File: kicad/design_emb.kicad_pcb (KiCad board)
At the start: 2 copper layers, 79.8 x 98.9 mm, 123 parts, among them J1 Conn_01x04, J2 Barrel_Jack, J3 USB_A, J4 Conn_01x03, J5 Conn_02x11_Counter_Clockwise, J6 Conn_02x10_Counter_Clockwise, J7 Screw_Terminal_01x02, J8 Screw_Terminal_01x02, K1 SANYOU_SRD_Form_C, K2 SANYOU_SRD_Form_C, Q1 MMBT3904, Q2 MMBT3904, SW1 SW_Push, SW3 SW_Push, U1 SRX.X.TCT, U10 S25FL116KOXNFIQ-11, U2 SRX.X.TCT, U3 STM32F446ZETx, U4 ICE40HX1K, U5 TLV1117LV33DCYR, U6 TLV1117LV33DCYR, U7 TLV1117LV12DCYR, U8 OMEGA2, U9 RCLAMP0502B

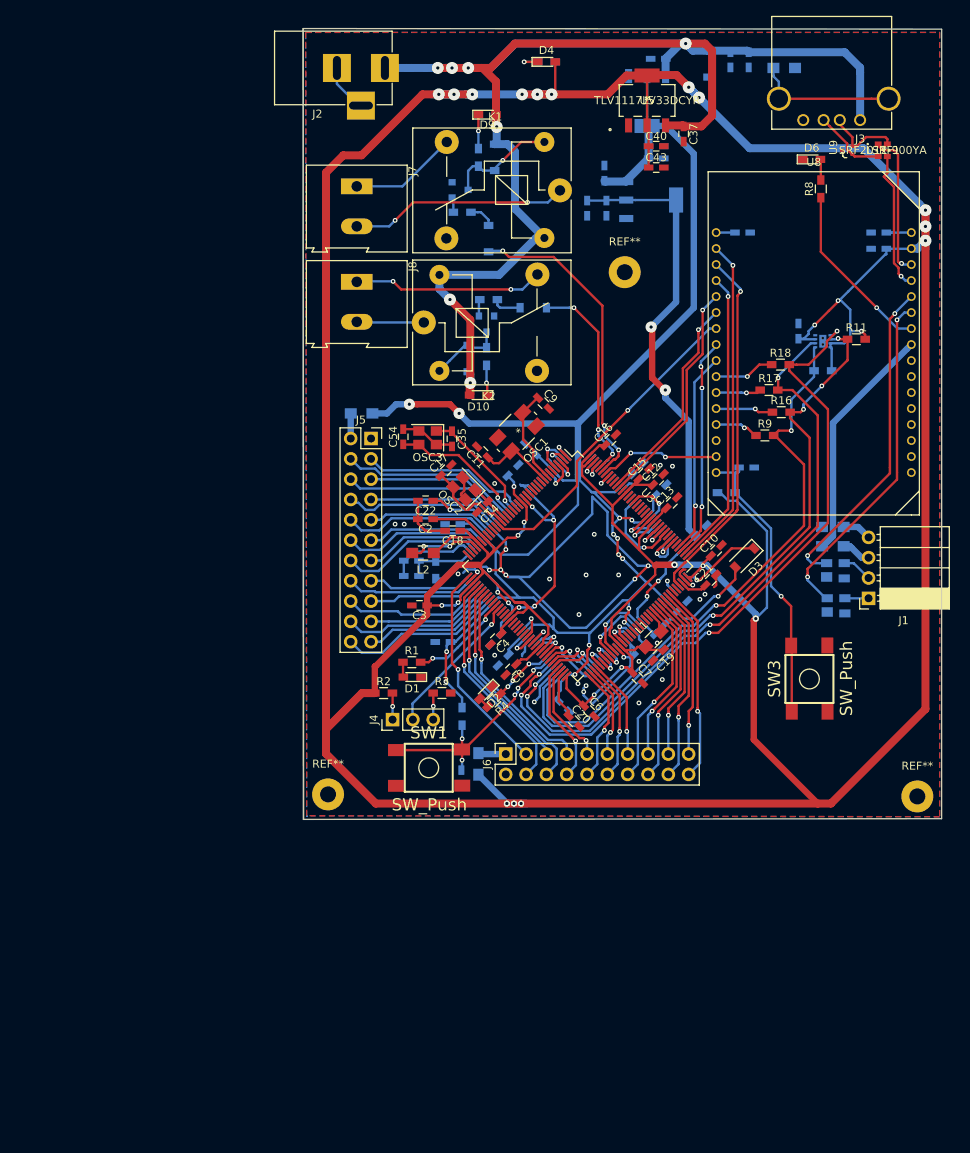
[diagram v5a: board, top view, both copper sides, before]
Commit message: correcciones silk
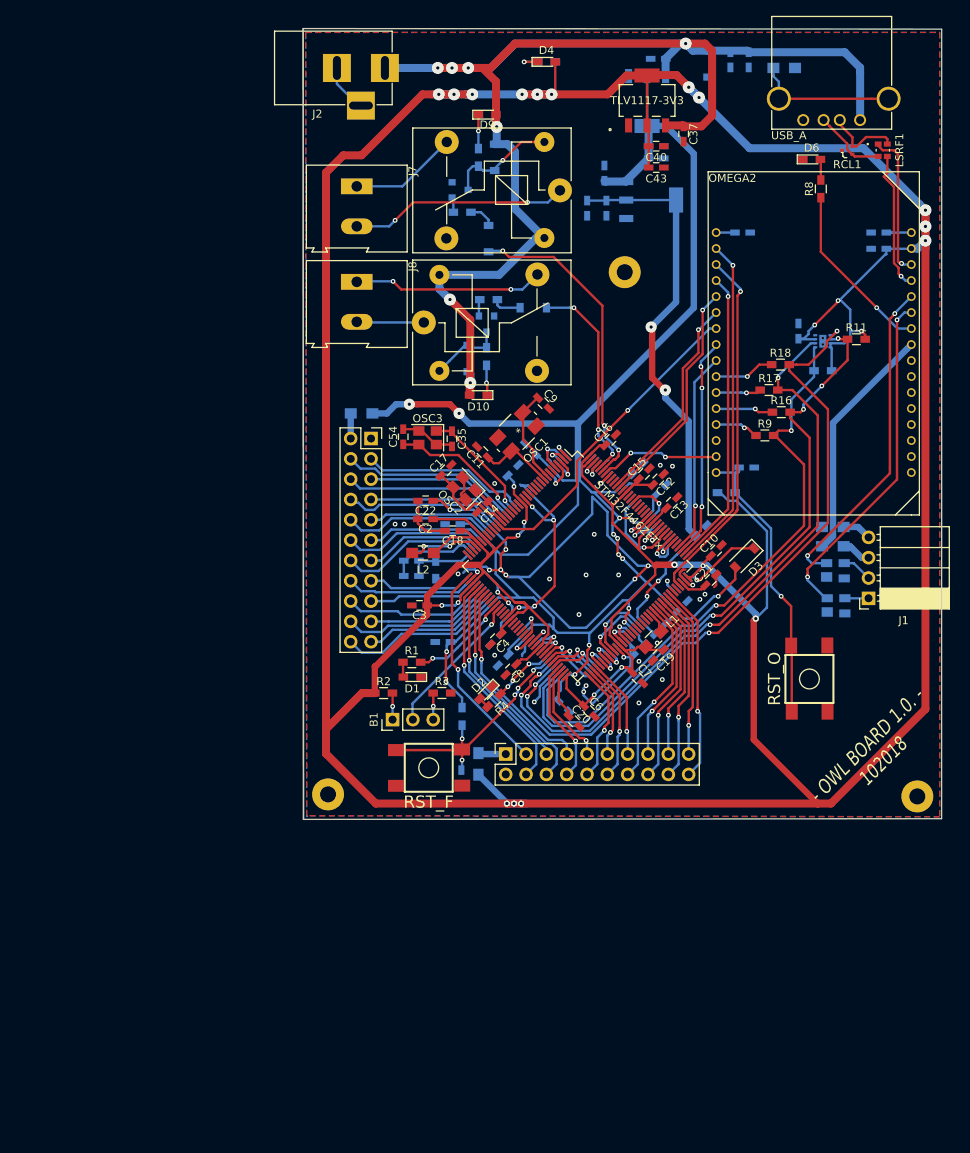
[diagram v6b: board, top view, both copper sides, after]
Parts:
- U5, U6: value TLV1117LV33DCYR -> TLV1117-3V3
- U7: value TLV1117LV12DCYR -> TLV1117-1V2
- renumbered J4 to B1, U4 to ICE40HX1K, U8 to OMEGA2, U9 to RCL1, SW1 to RST_F, SW3 to RST_O, U1 to SRX.X., U2 to SRX.X., U3 to STM32F446ZETx, J3 to USB_A
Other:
- board text added: "- OWL BOARD 1.0. - 102018"

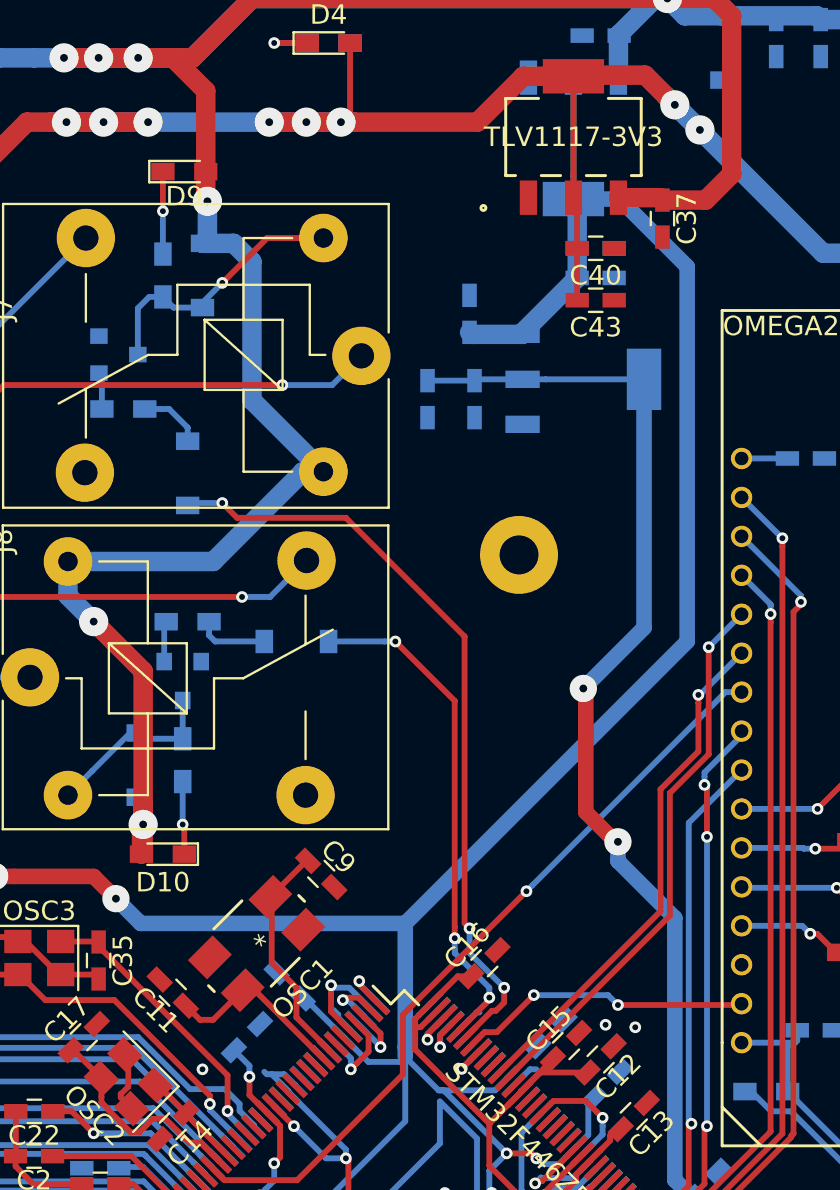
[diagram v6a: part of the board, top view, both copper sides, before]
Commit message: cambio osc1 stm32
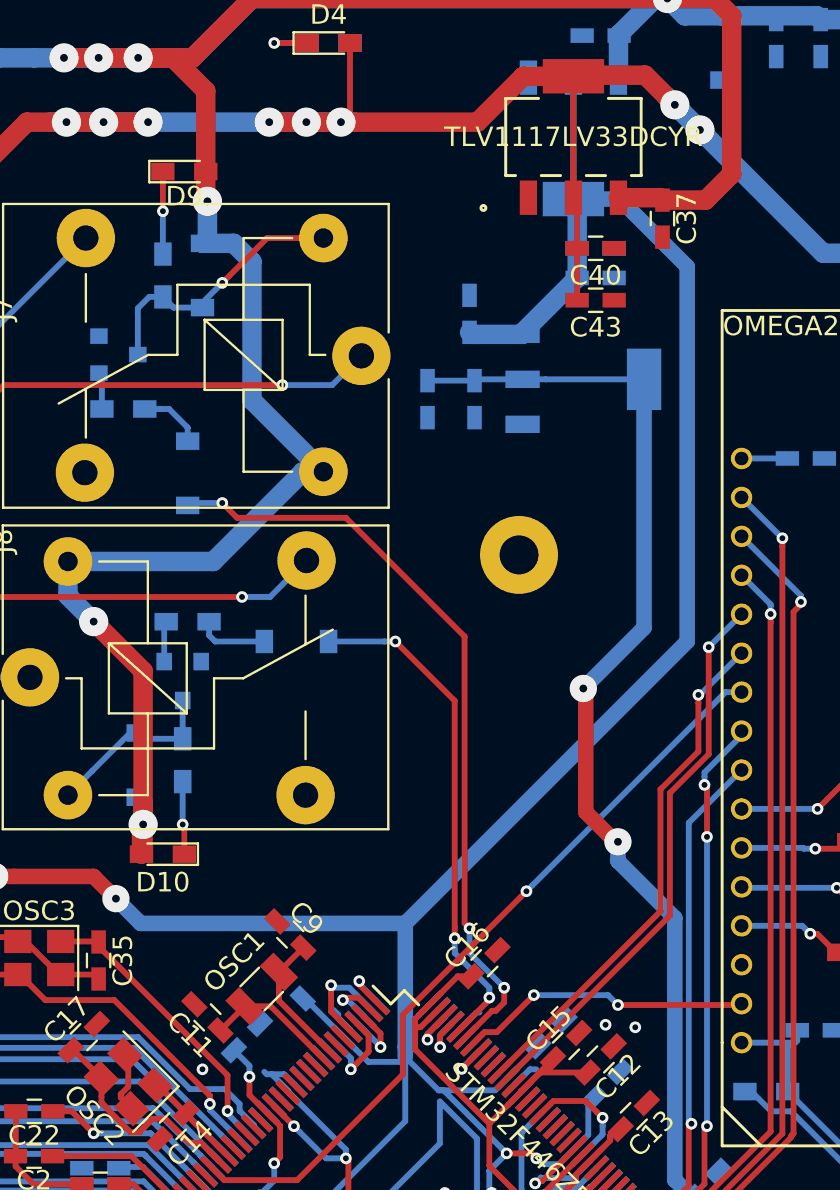
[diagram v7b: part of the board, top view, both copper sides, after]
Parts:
- C11, C9: value 18pF -> 9pF
- OSC1: value 32.768MHz -> 32,768K; footprint ABMM2-32.768MHZ:ABMM2-32.768MHZ-E2F-T -> Crystal:Crystal_SMD_3215-2Pin_3.2x1.5mm
- U5, U6: value TLV1117-3V3 -> TLV1117LV33DCYR
- U7: value TLV1117-1V2 -> TLV1117LV12DCYR
- moved C9 3.49 mm to (139.9, 94.3), turned to 135 degrees
- moved OSC1 2.37 mm to (138.4, 97.1), turned to 45 degrees
- moved C11 2.18 mm to (135.6, 98.6)
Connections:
- OSC1 pad 2: GND -> /Sheet1/OSC32_OUT
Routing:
- net /Sheet1/OSC32_IN: track 11.9 -> 6.91 mm
- net /Sheet1/OSC32_OUT: track 9.38 -> 6.85 mm
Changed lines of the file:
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@@
     (thickness 1.6)
     (drawings 7)
-    (tracks 1758)
+    (tracks 1753)
     (zones 0)
     (modules 123)
@@
   )
   (page A4)
+  (title_block
+    (title "OWL_BOARD 1.0.")
+    (date 10/2018)
+    (company "Fabio Segura")
+    (comment 1 "de la Maestría en Ingeniería Electrónica de la Universidad Nacional de Colombia")
+    (comment 2 "Tarjeta diseñada para la asiganatura \"Diseño e implementación de sistemas embebidos\"")
+  )
   (layers
     (0 F.Cu signal)
@@
     (add_net "Net-(U8-Pad24)")
   )
+  (module Crystal:Crystal_SMD_3215-2Pin_3.2x1.5mm (layer F.Cu)
+    (at 138.424883 97.096617 45)
+    (descr "SMD Crystal FC-135 https://support.epson.biz/td/api/doc_check.php?dl=brief_FC-135R_en.pdf")
+    (tags "SMD SMT Crystal")
+    (attr smd)
+    (fp_text reference OSC1 (at 0 -2 45) (layer F.SilkS)
+      (effects (font (size 1 1) (thickness 0.15)))
+    )
+    (fp_text value 32,768K (at 0 2 45) (layer F.Fab)
+      (effects (font (size 1 1) (thickness 0.15)))
+    )
+    (fp_line (start 2 -1.15) (end 2 1.15) (layer F.CrtYd) (width 0.05))
+    (fp_line (start -2 -1.15) (end -2 1.15) (layer F.CrtYd) (width 0.05))
+    (fp_line (start -2 1.15) (end 2 1.15) (layer F.CrtYd) (width 0.05))
+    (fp_line (start -1.6 0.75) (end 1.6 0.75) (layer F.Fab) (width 0.1))
+    (fp_line (start -1.6 -0.75) (end 1.6 -0.75) (layer F.Fab) (width 0.1))
+    (fp_line (start 1.6 -0.75) (end 1.6 0.75) (layer F.Fab) (width 0.1))
+    (fp_line (start -0.675 -0.875) (end 0.675 -0.875) (layer F.SilkS) (width 0.12))
+    (fp_line (start -0.675 0.875) (end 0.675 0.875) (layer F.SilkS) (width 0.12))
+    (fp_line (start -1.6 -0.75) (end -1.6 0.75) (layer F.Fab) (width 0.1))
+    (fp_line (start -2 -1.15) (end 2 -1.15) (layer F.CrtYd) (width 0.05))
+    (fp_text user %R (at 0 -2 45) (layer F.Fab)
+      (effects (font (size 1 1) (thickness 0.15)))
+    )
+    (pad 2 smd rect (at -1.25 0 45) (size 1 1.8) (layers F.Cu F.Paste F.Mask)
+      (net 3 /Sheet1/OSC32_OUT))
+    (pad 1 smd rect (at 1.25 0 45) (size 1 1.8) (layers F.Cu F.Paste F.Mask)
+      (net 2 /Sheet1/OSC32_IN))
+    (model ${KISYS3DMOD}/Crystal.3dshapes/Crystal_SMD_3215-2Pin_3.2x1.5mm.wrl
+      (at (xyz 0 0 0))
+      (scale (xyz 1 1 1))
+      (rotate (xyz 0 0 0))
+    )
+  )
   (module Wire_Pads:SolderWirePad_single_2mmDrill (layer F.Cu)
     (at 151.638 74.803)
@@
   )
   (module Capacitors_SMD:C_0603_HandSoldering (layer F.Cu)
-    (at 141.478 91.186 315)
+    (at 139.8905 94.2975 135)
     (descr "Capacitor SMD 0603, hand soldering")
     (tags "capacitor 0603")
     (attr smd)
-    (fp_text reference C9 (at 0 -1.25 315) (layer F.SilkS)
+    (fp_text reference C9 (at 0 1.167433 135) (layer F.SilkS)
       (effects (font (size 1 1) (thickness 0.15)))
     )
-    (fp_text value 18pF (at 0 1.5 315) (layer F.Fab)
+    (fp_text value 9pF (at 0 1.5 135) (layer F.Fab)
       (effects (font (size 1 1) (thickness 0.15)))
     )
-    (fp_text user %R (at 0 -1.249999 315) (layer F.Fab)
+    (fp_text user %R (at 0 -1.249999 135) (layer F.Fab)
       (effects (font (size 1 1) (thickness 0.15)))
     )
@@
     (fp_line (start 1.8 0.65) (end 1.8 -0.65) (layer F.CrtYd) (width 0.05))
     (fp_line (start 1.8 0.65) (end -1.8 0.65) (layer F.CrtYd) (width 0.05))
-    (pad 1 smd rect (at -0.949999 0 315) (size 1.2 0.75) (layers F.Cu F.Paste F.Mask)
+    (pad 1 smd rect (at -0.949999 0 135) (size 1.2 0.75) (layers F.Cu F.Paste F.Mask)
       (net 2 /Sheet1/OSC32_IN))
-    (pad 2 smd rect (at 0.949999 0 315) (size 1.2 0.75) (layers F.Cu F.Paste F.Mask)
+    (pad 2 smd rect (at 0.949999 0 135) (size 1.2 0.75) (layers F.Cu F.Paste F.Mask)
       (net 1 GND))
     (model Capacitors_SMD.3dshapes/C_0603.wrl
@@
   )
   (module Capacitors_SMD:C_0603_HandSoldering (layer F.Cu)
-    (at 133.858 97.282 135)
+    (at 135.636 98.552 135)
     (descr "Capacitor SMD 0603, hand soldering")
     (tags "capacitor 0603")
@@
       (effects (font (size 1 1) (thickness 0.15)))
     )
-    (fp_text value 18pF (at 0 1.5 135) (layer F.Fab)
+    (fp_text value 9pF (at 0 1.5 135) (layer F.Fab)
       (effects (font (size 1 1) (thickness 0.15)))
     )
@@
       (net 30 "Net-(J3-Pad2)"))
   )
-  (module ABMM2-32.768MHZ:ABMM2-32.768MHZ-E2F-T (layer F.Cu)
-    (at 138.176 94.742 225)
-    (fp_text reference OSC1 (at 0 -3.302 45) (layer F.SilkS)
-      (effects (font (size 1 1) (thickness 0.15)))
-    )
-    (fp_text value 32.768MHz (at 0 3.429 45) (layer F.SilkS) hide
-      (effects (font (size 1 1) (thickness 0.15)))
-    )
-    (fp_text user "Copyright 2016 Accelerated Designs. All rights reserved." (at 0.025401 0 -45) (layer Cmts.User)
-      (effects (font (size 0.127 0.127) (thickness 0.002)))
-    )
-    (fp_text user * (at 0.025401 0 -45) (layer F.SilkS)
-      (effects (font (size 1 1) (thickness 0.15)))
-    )
-    (fp_text user * (at 0.025401 0 -45) (layer F.Fab)
-      (effects (font (size 1 1) (thickness 0.15)))
-    )
-    (fp_line (start 3.302001 0.214047) (end 3.302001 -0.214047) (layer F.SilkS) (width 0.1524))
-    (fp_line (start 1.047989 -2.0828) (end -0.997189 -2.0828) (layer F.SilkS) (width 0.1524))
-    (fp_line (start -3.2512 -0.214048) (end -3.2512 0.214048) (layer F.SilkS) (width 0.1524))
-    (fp_line (start -0.997189 2.0828) (end 1.047989 2.0828) (layer F.SilkS) (width 0.1524))
-    (fp_line (start 3.175 1.955799) (end 3.175 -1.955799) (layer F.Fab) (width 0.1524))
-    (fp_line (start 3.175 -1.955799) (end -3.1242 -1.955799) (layer F.Fab) (width 0.1524))
-    (fp_line (start -3.1242 -1.955799) (end -3.1242 1.955799) (layer F.Fab) (width 0.1524))
-    (fp_line (start -3.1242 1.955799) (end 3.175 1.955799) (layer F.Fab) (width 0.1524))
-    (fp_line (start 3.429 2.2098) (end -3.378201 2.2098) (layer F.CrtYd) (width 0.1524))
-    (fp_line (start -3.378201 2.2098) (end -3.378201 -2.2098) (layer F.CrtYd) (width 0.1524))
-    (fp_line (start -3.378201 -2.2098) (end 3.429 -2.2098) (layer F.CrtYd) (width 0.1524))
-    (fp_line (start 3.429 -2.2098) (end 3.429 2.2098) (layer F.CrtYd) (width 0.1524))
-    (fp_arc (start -3.1242 0) (end -3.1242 -0.3048) (angle 180) (layer F.Fab) (width 0.1524))
-    (pad 1 smd rect (at -2.1717 1.1938 315) (size 1.397 1.8034) (layers F.Cu F.Paste F.Mask)
-      (net 2 /Sheet1/OSC32_IN))
-    (pad 2 smd rect (at 2.2225 1.1938 315) (size 1.397 1.8034) (layers F.Cu F.Paste F.Mask)
-      (net 1 GND))
-    (pad 3 smd rect (at 2.2225 -1.1938 315) (size 1.397 1.8034) (layers F.Cu F.Paste F.Mask)
-      (net 3 /Sheet1/OSC32_OUT))
-    (pad 4 smd rect (at -2.1717 -1.1938 315) (size 1.397 1.8034) (layers F.Cu F.Paste F.Mask)
-      (net 1 GND))
-  )
   (module Crystals:Crystal_SMD_Abracon_ABM8G-4pin_3.2x2.5mm (layer F.Cu)
     (at 131.572 101.854 135)
@@
       (effects (font (size 1 1) (thickness 0.15)))
     )
-    (fp_text value TLV1117-3V3 (at 0 0) (layer F.SilkS)
+    (fp_text value TLV1117LV33DCYR (at 0 0) (layer F.SilkS)
       (effects (font (size 1 1) (thickness 0.15)))
     )
@@
       (effects (font (size 1 1) (thickness 0.15)) (justify mirror))
     )
-    (fp_text value TLV1117-3V3 (at 0 0) (layer B.SilkS)
+    (fp_text value TLV1117LV33DCYR (at 0 0) (layer B.SilkS)
       (effects (font (size 1 1) (thickness 0.15)) (justify mirror))
     )
@@
       (effects (font (size 1 1) (thickness 0.15)) (justify mirror))
     )
-    (fp_text value TLV1117-1V2 (at 0 0 90) (layer B.SilkS)
+    (fp_text value TLV1117LV12DCYR (at 0 0 90) (layer B.SilkS)
       (effects (font (size 1 0.9) (thickness 0.15)) (justify mirror))
     )
@@
   (segment (start 141.732 105.791) (end 142.748 105.791) (width 0.3) (layer B.Cu) (net 1))
   (segment (start 140.081 104.14) (end 141.732 105.791) (width 0.3) (layer B.Cu) (net 1))
-  (segment (start 140.715463 90.514249) (end 140.806249 90.514249) (width 0.3) (layer F.Cu) (net 2))
-  (segment (start 138.86748 92.362232) (end 140.715463 90.514249) (width 0.3) (layer F.Cu) (net 2))
-  (segment (start 138.938 95.758) (end 138.938 92.432752) (width 0.3) (layer F.Cu) (net 2))
-  (segment (start 138.938 92.432752) (end 138.86748 92.362232) (width 0.3) (layer F.Cu) (net 2))
-  (segment (start 141.894225 100.281869) (end 141.894225 100.238225) (width 0.3) (layer F.Cu) (net 2))
-  (segment (start 141.894225 100.238225) (end 140.208 98.552) (width 0.3) (layer F.Cu) (net 2))
-  (segment (start 140.208 98.552) (end 140.208 97.028) (width 0.3) (layer F.Cu) (net 2))
-  (segment (start 140.208 97.028) (end 138.938 95.758) (width 0.3) (layer F.Cu) (net 2))
-  (segment (start 138.062939 97.157689) (end 137.448599 97.157689) (width 0.3) (layer F.Cu) (net 3))
-  (segment (start 141.540672 100.635422) (end 138.062939 97.157689) (width 0.3) (layer F.Cu) (net 3))
-  (segment (start 135.255 98.679) (end 134.529751 97.953751) (width 0.3) (layer F.Cu) (net 3))
-  (segment (start 135.927288 98.679) (end 135.255 98.679) (width 0.3) (layer F.Cu) (net 3))
-  (segment (start 137.448599 97.157689) (end 135.927288 98.679) (width 0.3) (layer F.Cu) (net 3))
+  (segment (start 139.308766 97.69641) (end 139.308766 96.212734) (width 0.3) (layer F.Cu) (net 2))
+  (segment (start 141.894225 100.281869) (end 139.308766 97.69641) (width 0.3) (layer F.Cu) (net 2))
+  (segment (start 139.318768 96.212734) (end 140.562251 94.969251) (width 0.3) (layer F.Cu) (net 2))
+  (segment (start 139.308766 96.212734) (end 139.318768 96.212734) (width 0.3) (layer F.Cu) (net 2))
+  (segment (start 138.88575 97.9805) (end 137.541 97.9805) (width 0.3) (layer F.Cu) (net 3))
+  (segment (start 141.540672 100.635422) (end 138.88575 97.9805) (width 0.3) (layer F.Cu) (net 3))
+  (segment (start 137.541 97.990502) (end 136.307751 99.223751) (width 0.3) (layer F.Cu) (net 3))
+  (segment (start 137.541 97.9805) (end 137.541 97.990502) (width 0.3) (layer F.Cu) (net 3))
   (segment (start 134.529751 103.523997) (end 134.529751 103.468249) (width 0.3) (layer F.Cu) (net 4))
   (segment (start 136.590924 105.58517) (end 134.529751 103.523997) (width 0.3) (layer F.Cu) (net 4))

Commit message: corrección errores DRC
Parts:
- moved C53 0.06 mm to (130.1, 106.2)
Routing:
- net /Sheet4/+1V2_FPGA: track 165.4 -> 163.9 mm
- net GND: track 93.3 -> 91.9 mm, vias 30 -> 66
